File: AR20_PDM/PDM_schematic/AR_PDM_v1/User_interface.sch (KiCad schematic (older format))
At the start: 73 parts, among them P1 B4B-PH-SM4-TB, U32 Fet-P, U33 Fet-P, U34 Fet-P, U35 Fet-P, U36 Fet-P

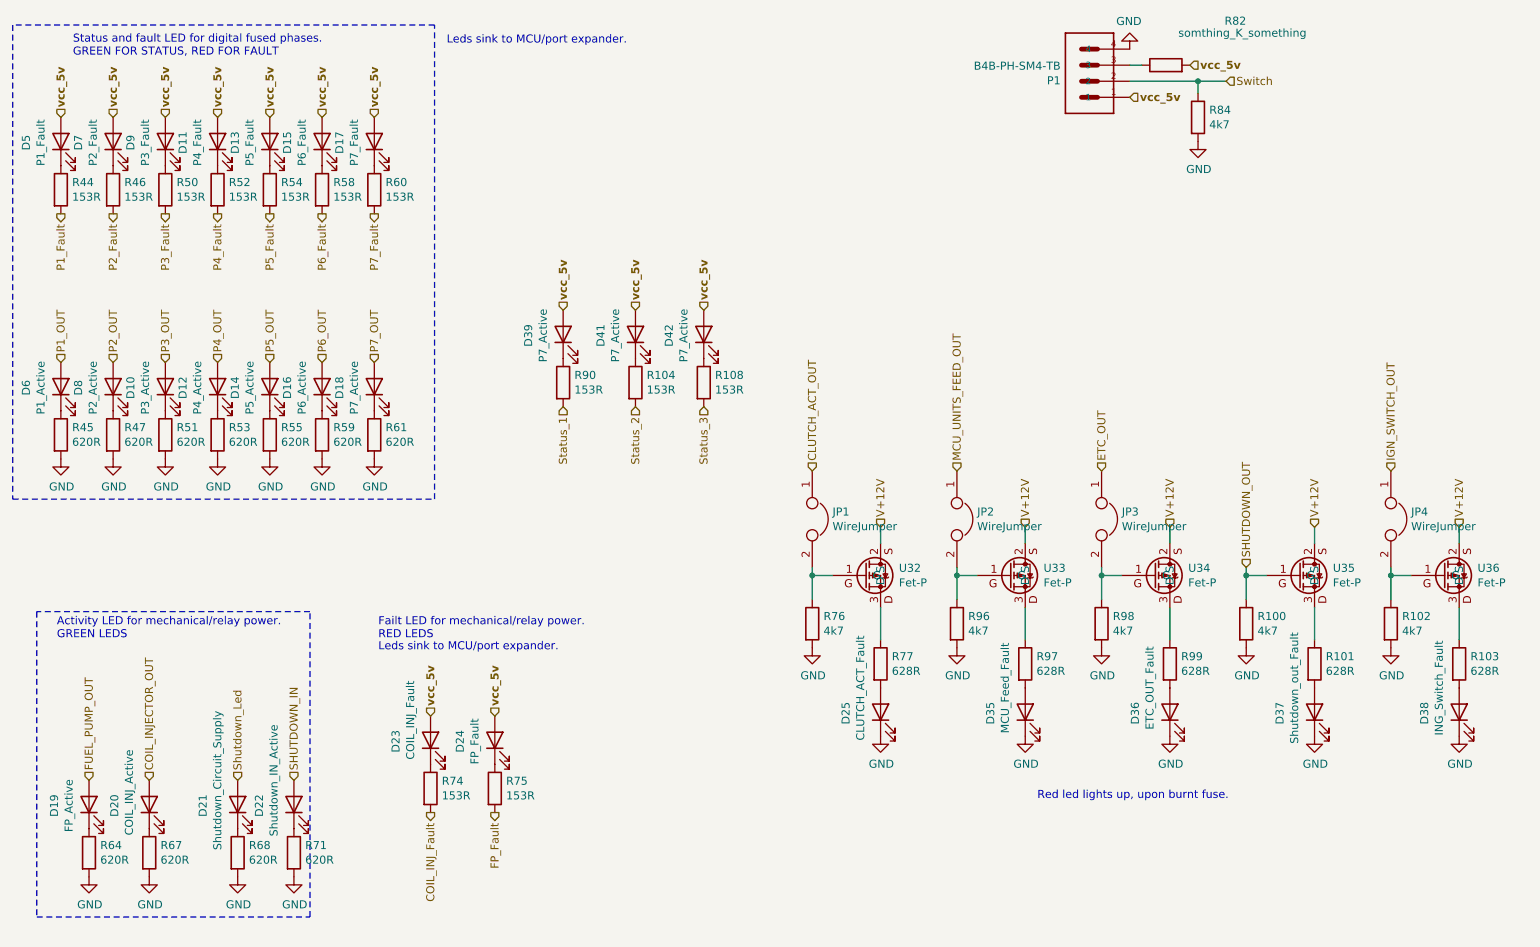
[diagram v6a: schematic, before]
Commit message: shematics adjustments, and fixing values and names
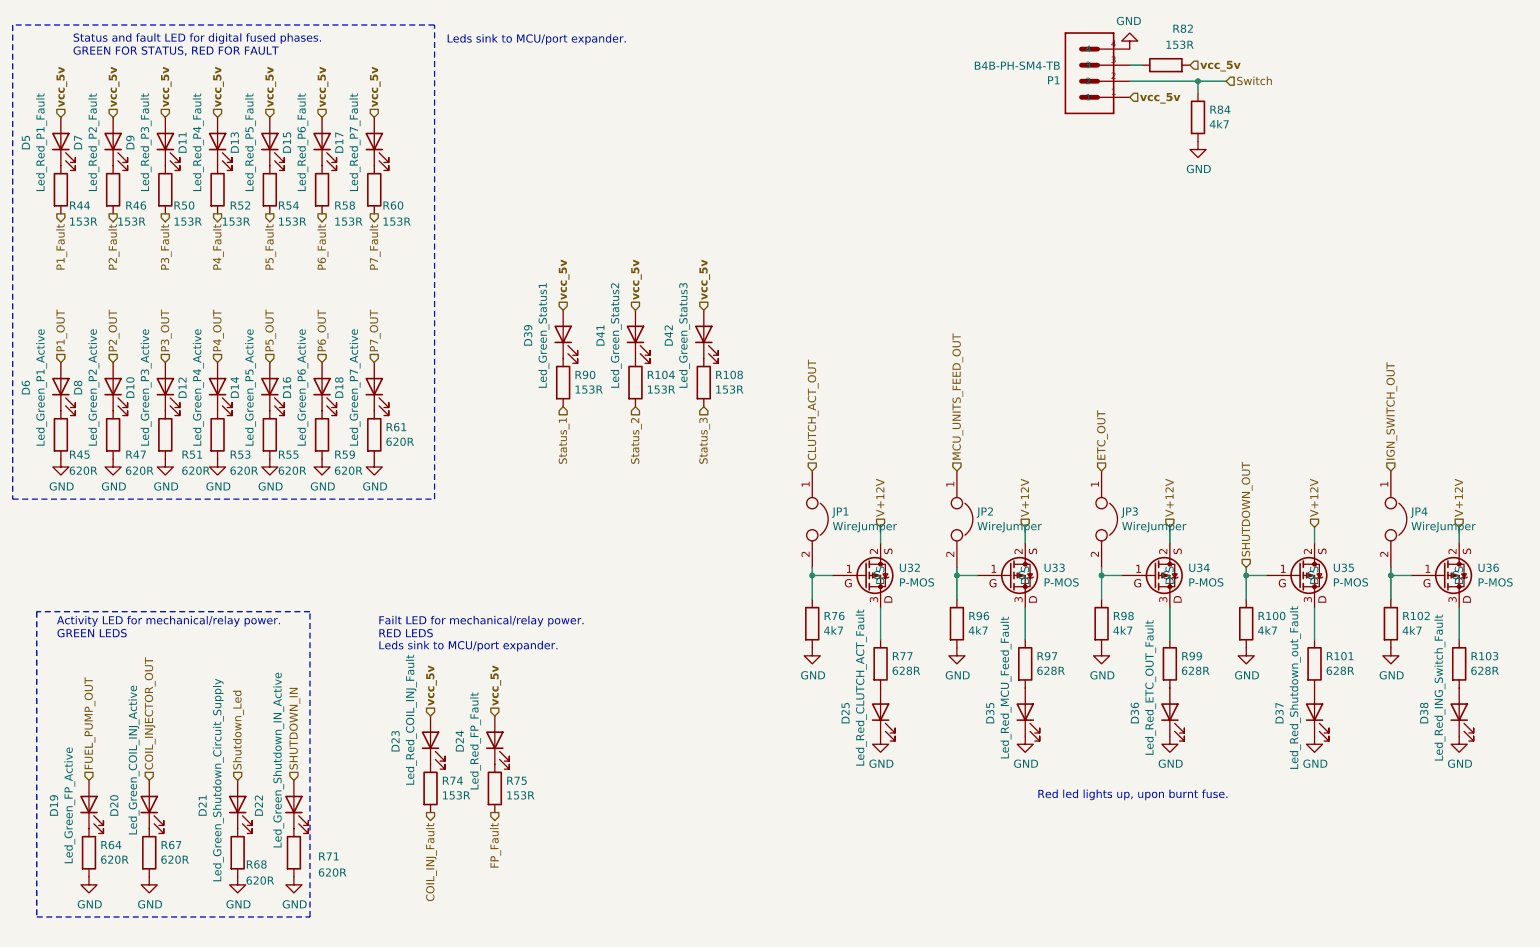
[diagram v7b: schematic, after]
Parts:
- D10: value P3_Active -> Led_Green_P3_Active
- D11: value P4_Fault -> Led_Red_P4_Fault
- D12: value P4_Active -> Led_Green_P4_Active
- D13: value P5_Fault -> Led_Red_P5_Fault
- D14: value P5_Active -> Led_Green_P5_Active
- D15: value P6_Fault -> Led_Red_P6_Fault
- D16: value P6_Active -> Led_Green_P6_Active
- D17: value P7_Fault -> Led_Red_P7_Fault
- D18: value P7_Active -> Led_Green_P7_Active
- D19: value FP_Active -> Led_Green_FP_Active
- D20: value COIL_INJ_Active -> Led_Green_COIL_INJ_Active
- D21: value Shutdown_Circuit_Supply -> Led_Green_Shutdown_Circuit_Supply
- D22: value Shutdown_IN_Active -> Led_Green_Shutdown_IN_Active
- D23: value COIL_INJ_Fault -> Led_Red_COIL_INJ_Fault
- D24: value FP_Fault -> Led_Red_FP_Fault
- D25: value CLUTCH_ACT_Fault -> Led_Red_CLUTCH_ACT_Fault
- D35: value MCU_Feed_Fault -> Led_Red_MCU_Feed_Fault
- D36: value ETC_OUT_Fault -> Led_Red_ETC_OUT_Fault
- D37: value Shutdown_out_Fault -> Led_Red_Shutdown_out_Fault
- D38: value ING_Switch_Fault -> Led_Red_ING_Switch_Fault
- D39: value P7_Active -> Led_Green_Status1
- D41: value P7_Active -> Led_Green_Status2
- D42: value P7_Active -> Led_Green_Status3
- D5: value P1_Fault -> Led_Red_P1_Fault
- D6: value P1_Active -> Led_Green_P1_Active
- D7: value P2_Fault -> Led_Red_P2_Fault
- D8: value P2_Active -> Led_Green_P2_Active
- D9: value P3_Fault -> Led_Red_P3_Fault
- R82: value somthing_K_something -> 153R
- U32, U33, U34, U35, U36: value Fet-P -> P-MOS

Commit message: Changer Led Resistor Values
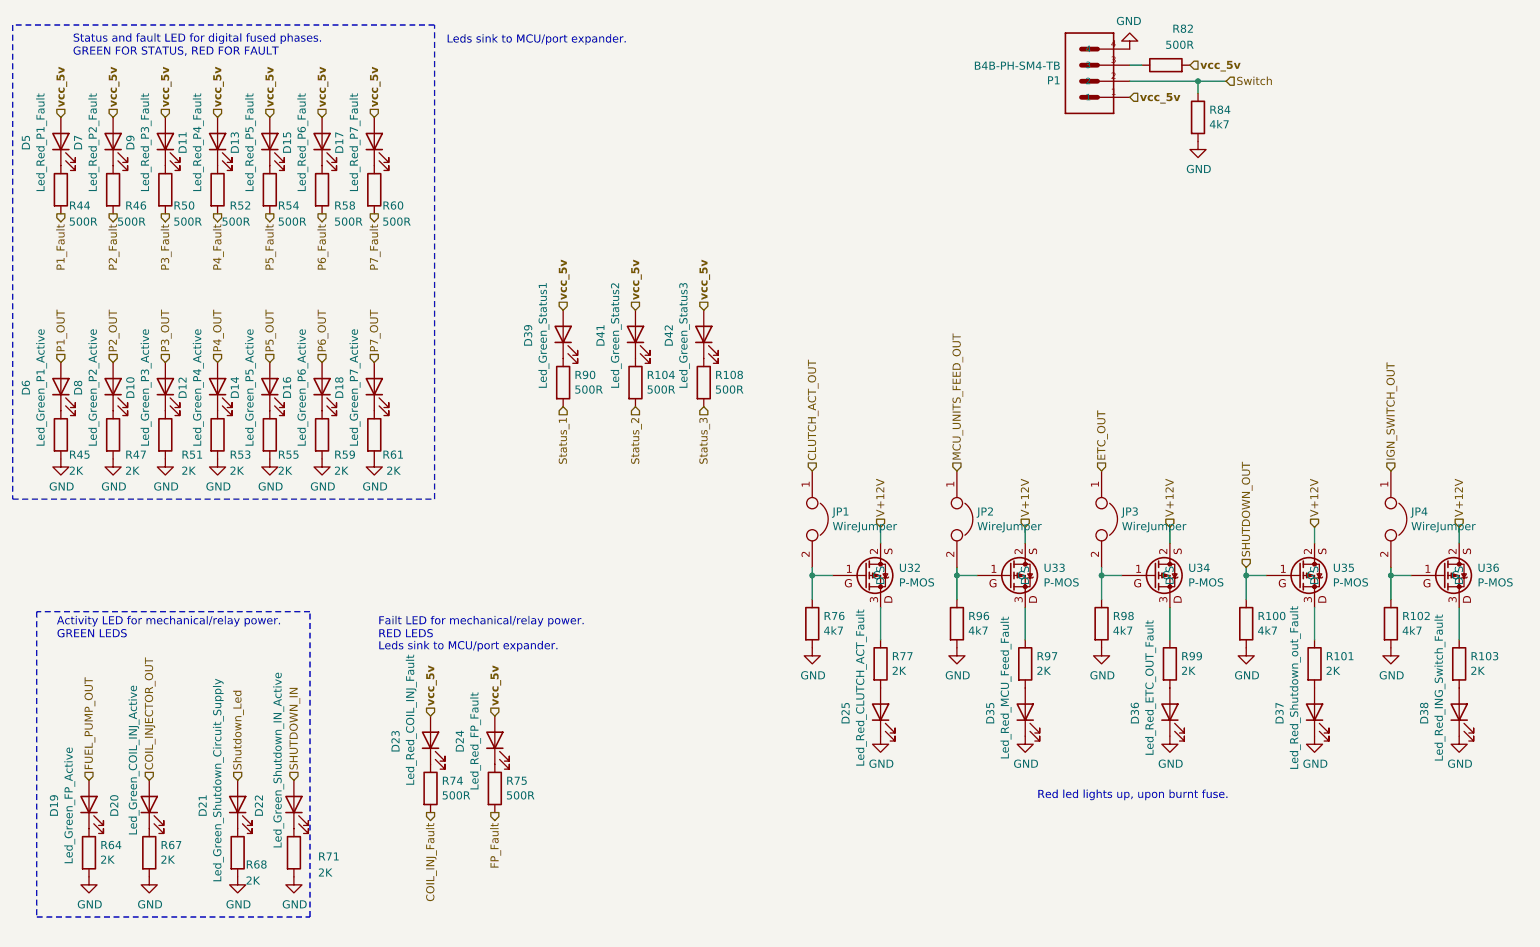
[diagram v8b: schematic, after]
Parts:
- R101, R103, R77, R97, R99: value 628R -> 2K
- R104, R108, R44, R46, R50, R52, R54, R58, R60, R74, R75, R82, R90: value 153R -> 500R
- R45, R47, R51, R53, R55, R59, R61, R64, R67, R68, R71: value 620R -> 2K
